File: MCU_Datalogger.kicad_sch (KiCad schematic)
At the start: 25 parts

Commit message: Schematic design complete
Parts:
- BT1: renamed from BT?; footprint (none) -> Connector_PinHeader_2.54mm:PinHeader_1x02_P2.54mm_Vertical
- C1, C4: renamed from C?; value C -> 0.1uF; footprint (none) -> Capacitor_SMD:C_0805_2012Metric_Pad1.18x1.45mm_HandSolder
- C2, C3: renamed from C?; value C -> 22pF; footprint (none) -> Capacitor_SMD:C_0805_2012Metric_Pad1.18x1.45mm_HandSolder
- C5: renamed from C?; value C_Polarized -> 100nF; footprint (none) -> Capacitor_SMD:C_0805_2012Metric_Pad1.18x1.45mm_HandSolder
- D1, D2: renamed from D?; footprint (none) -> LED_SMD:LED_0805_2012Metric_Pad1.15x1.40mm_HandSolder
- H1, H2, H3, H4: renamed from H?; footprint (none) -> MountingHole:MountingHole_2.1mm
- R1, R2, R6: renamed from R?; value R_US -> 10K; footprint (none) -> Resistor_SMD:R_0805_2012Metric_Pad1.20x1.40mm_HandSolder
- R3, R5: renamed from R?; value R_US -> 4.7K; footprint (none) -> Resistor_SMD:R_0805_2012Metric_Pad1.20x1.40mm_HandSolder
- R4, R7: renamed from R?; value R_US -> 330; footprint (none) -> Resistor_SMD:R_0805_2012Metric_Pad1.20x1.40mm_HandSolder
- U1: renamed from U?; footprint SOIC127P600X175-8N -> DS1337S_:SOIC127P600X175-8N
- U2, U3: renamed from U?; footprint (none) -> Package_SO:SOIC-8_5.23x5.23mm_P1.27mm
- U4: renamed from U?; footprint QFP80P900X900X120-32N -> ATMEGA328P-AU:QFP80P900X900X120-32N
- Y1: renamed from Y?; value Crystal -> 32.768 KHz; footprint (none) -> Crystal:Crystal_SMD_5032-2Pin_5.0x3.2mm_HandSoldering
- Y2: renamed from Y?; value Crystal -> 16 MHz; footprint (none) -> Crystal:Crystal_SMD_5032-2Pin_5.0x3.2mm_HandSoldering
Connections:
- net Vcc: now reaches R5.1
- net Vcc: now also C1.1, R1.1, R2.1, R3.1, R6.1, U1.8 (VCC), U2.1 (A0), U2.2 (A1), U2.3 (A2), U2.8 (VCC), U3.1 (A0), U3.3 (A2), U3.8 (VCC)
- net SDA: now reaches R5.2
- net SDA: now also U1.5 (SDA), U2.5 (SDA), U3.5 (SDA), U4.27 (PC4)
- net GND: now reaches C1.2
- net GND: now also BT1.2 (-), C2.1, C3.1, C4.1, C5.2, R4.1, R7.2, U1.4 (GND), U2.4 (GND), U2.7 (WP), U3.2 (A1), U3.4 (GND), U3.7 (WP), U4.21 (GND), U4.3 (GND), U4.5 (GND)
- net SCK: now reaches U2.6 (SCL)
- net SCK: now also D1.2 (A), R3.2, U1.6 (SCL), U3.6 (SCL), U4.17 (PB5), U4.28 (PC5)
- net at D1.1 (K): now also R4.2
- net at R7.1: now also D2.1 (K)
- net at U1.1 (X1): now also Y1.1
- net at U1.2 (X2): now also Y1.2
- net at U1.3 (~{INTA}): now also R1.2
- net at U1.7 (SQW/~{INT}): now also R2.2
- net at Y2.1: now also C3.2, U4.8 (PB7)
- net at Y2.2: now also C2.2, U4.7 (PB6)
- net D3: now reaches U4.1 (PD3)
- net D6: now reaches U4.10 (PD6)
- net D7: now reaches U4.11 (PD7)
- net D8: now reaches U4.12 (PB0)
- net MOSI: now reaches U4.15 (PB3)
- net MISO: now reaches U4.16 (PB4)
- net at U4.18 (AVCC): now also BT1.1 (+), C5.1, D2.2 (A), U4.4 (VCC)
- net D4: now reaches U4.2 (PD4)
- net at U4.20 (AREF): now also C4.2
- net RESET: now reaches U4.29 (PC6/~{RESET})
- net RESET: now also R6.2
- net RX: now reaches U4.30 (PD0)
- net TX: now reaches U4.31 (PD1)
- net D2: now reaches U4.32 (PD2)
- net at U4.6 (VCC): no longer U4.4 (VCC)
- net D5: now reaches U4.9 (PD5)
- no-connect marks 0 -> 9
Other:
- sheet Connectors ports: added D2, D3, D4, D5, D6, D7, D8, GND, MISO, MOSI, RESET, RX, SCK, SDA, TX, Vcc; removed none
- note added: "EEPROM"
- note added: "MCU"
- note added: "Real Time Clock"
- moved on the sheet: BT1, C1, C2, C3, C4, C5, D1, D2, H1, H2, H3, H4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

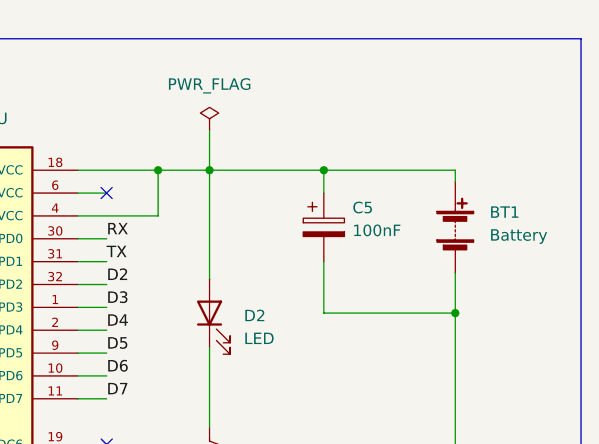
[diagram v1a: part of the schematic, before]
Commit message: 2 layer PCB design complete
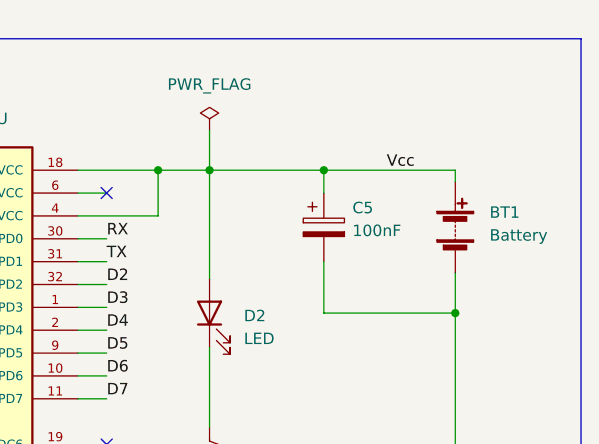
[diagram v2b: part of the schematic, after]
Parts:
- Y1, Y2: footprint Crystal:Crystal_SMD_5032-2Pin_5.0x3.2mm_HandSoldering -> ABM2-32:XTAL_ABM2-32.000MHZ-D4YF-T
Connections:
- net Vcc: now also BT1.1 (+), C5.1, D2.2 (A), U4.18 (AVCC), U4.4 (VCC)
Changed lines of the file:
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@@
+    (effects (font (size 1.27 1.27)) (justify left bottom))
+  )
+  (label "Vcc" (at 256.54 43.18 0)
     (effects (font (size 1.27 1.27)) (justify left bottom))
   )
@@
       (effects (font (size 1.27 1.27)) (justify right))
     )
-    (property "Footprint" "Crystal:Crystal_SMD_5032-2Pin_5.0x3.2mm_HandSoldering" (id 2) (at 169.545 71.755 0)
+    (property "Footprint" "ABM2-32:XTAL_ABM2-32.000MHZ-D4YF-T" (id 2) (at 169.545 71.755 0)
       (effects (font (size 1.27 1.27)) hide)
     )
@@
       (effects (font (size 1.27 1.27)) (justify left))
     )
-    (property "Footprint" "Crystal:Crystal_SMD_5032-2Pin_5.0x3.2mm_HandSoldering" (id 2) (at 21.59 69.85 0)
+    (property "Footprint" "ABM2-32:XTAL_ABM2-32.000MHZ-D4YF-T" (id 2) (at 21.59 69.85 0)
       (effects (font (size 1.27 1.27)) hide)
     )
@@
     )
     (path "/c96d047b-f1e3-4e27-aa7a-e20f3d748e34"
-      (reference "Y1") (unit 1) (value "32.768 KHz") (footprint "Crystal:Crystal_SMD_5032-2Pin_5.0x3.2mm_HandSoldering")
+      (reference "Y1") (unit 1) (value "32.768 KHz") (footprint "ABM2-32:XTAL_ABM2-32.000MHZ-D4YF-T")
     )
     (path "/780593a8-3f7b-4d23-9ea7-1f7af43d16ab"
-      (reference "Y2") (unit 1) (value "16 MHz") (footprint "Crystal:Crystal_SMD_5032-2Pin_5.0x3.2mm_HandSoldering")
-    )
-  )
+      (reference "Y2") (unit 1) (value "16 MHz") (footprint "ABM2-32:XTAL_ABM2-32.000MHZ-D4YF-T")
+    )
+  )

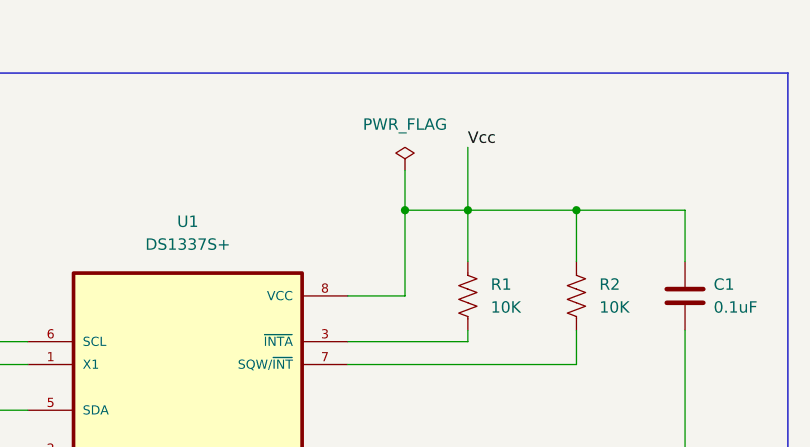
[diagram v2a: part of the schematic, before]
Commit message: Minor changes to PCB footprints
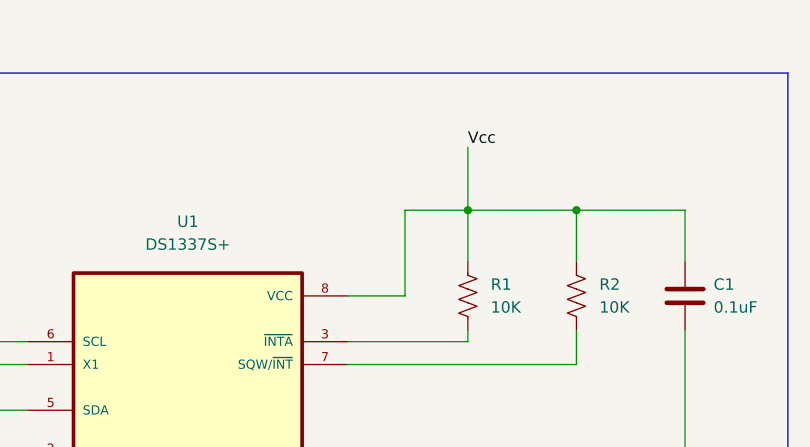
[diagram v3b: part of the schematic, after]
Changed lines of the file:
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@@
   (junction (at 169.545 76.835) (diameter 0) (color 0 0 0 0)
-  )
-  (junction (at 90.805 47.625) (diameter 0) (color 0 0 0 0)
   )
   (junction (at 146.685 53.34) (diameter 0) (color 0 0 0 0)
@@
   )
   (wire (pts (xy 197.485 129.54) (xy 181.61 129.54))
-    (stroke (width 0) (type default) (color 0 0 0 0))
-  )
-  (wire (pts (xy 90.805 43.18) (xy 90.805 47.625))
     (stroke (width 0) (type default) (color 0 0 0 0))
   )
@@
     (pin "1")
   )
-  (symbol (lib_id "power:PWR_FLAG") (at 90.805 43.18 0) (unit 1)
-    (in_bom yes) (on_board yes) (fields_autoplaced)
-    (property "Reference" "#FLG0103" (id 0) (at 90.805 41.275 0)
-      (effects (font (size 1.27 1.27)) hide)
-    )
-    (property "Value" "PWR_FLAG" (id 1) (at 90.805 38.1 0))
-    (property "Footprint" "" (id 2) (at 90.805 43.18 0)
-      (effects (font (size 1.27 1.27)) hide)
-    )
-    (property "Datasheet" "~" (id 3) (at 90.805 43.18 0)
-      (effects (font (size 1.27 1.27)) hide)
-    )
-    (pin "1")
-  )
   (symbol (lib_id "Device:R_US") (at 178.435 88.9 90) (unit 1)
     (in_bom yes) (on_board yes) (fields_autoplaced)
@@
       (reference "#FLG0102") (unit 1) (value "PWR_FLAG") (footprint "")
     )
-    (path "/f020a6f4-caee-4c19-8fba-99f271eb778b"
-      (reference "#FLG0103") (unit 1) (value "PWR_FLAG") (footprint "")
-    )
     (path "/e30ba7ec-fa95-461f-beca-d2c08d6124f6"

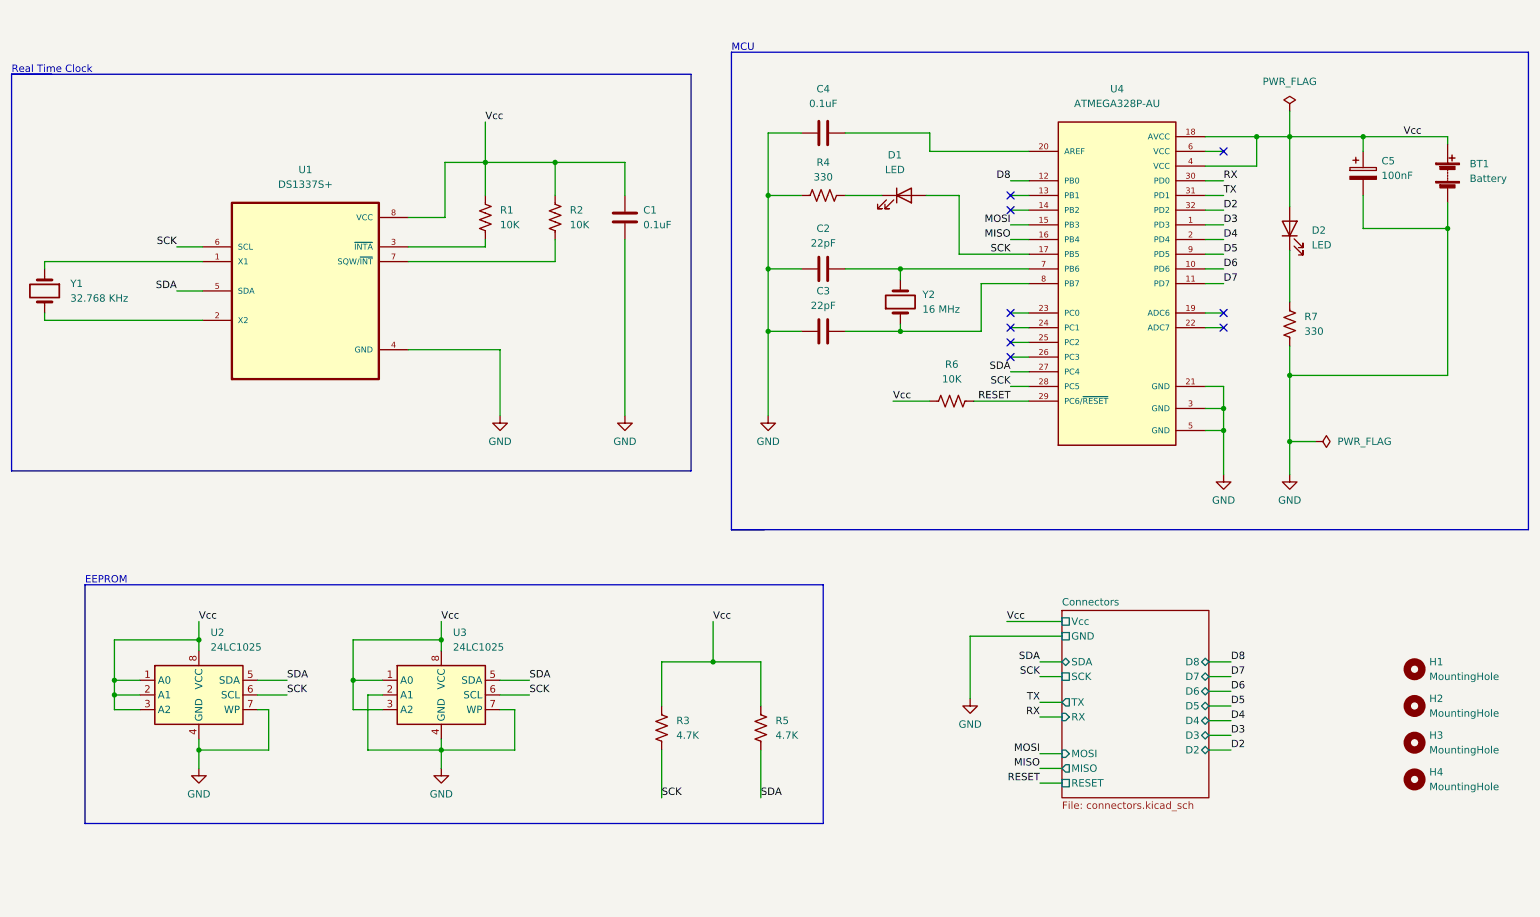
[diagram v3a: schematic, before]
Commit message: Added SCL net to schematic and fixed errors
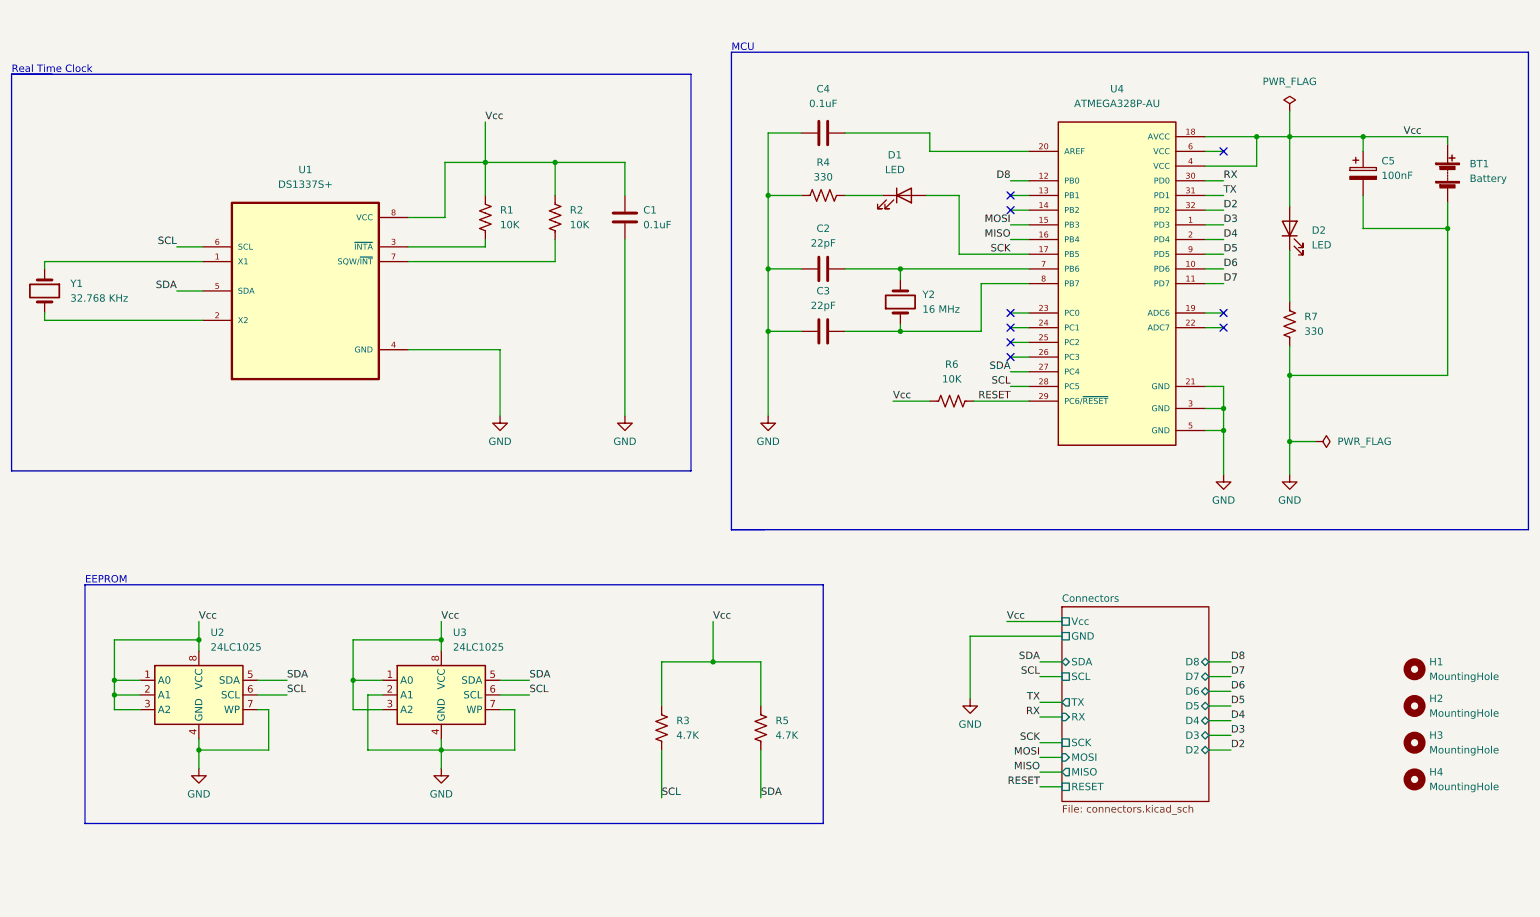
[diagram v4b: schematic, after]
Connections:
- net SCK: no longer R3.2, U1.6 (SCL), U2.6 (SCL), U3.6 (SCL), U4.28 (PC5)
- new net SCL: R3.2, U1.6 (SCL), U2.6 (SCL), U3.6 (SCL), U4.28 (PC5)
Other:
- sheet Connectors ports: added SCL; removed none
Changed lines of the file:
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@@
     (stroke (width 0) (type default) (color 0 0 0 0))
   )
-  (wire (pts (xy 193.675 154.94) (xy 197.485 154.94))
+  (wire (pts (xy 193.675 155.575) (xy 197.485 155.575))
     (stroke (width 0) (type default) (color 0 0 0 0))
   )
@@
     (stroke (width 0) (type default) (color 0 0 0 0))
   )
-  (wire (pts (xy 193.675 149.86) (xy 197.485 149.86))
+  (wire (pts (xy 193.675 150.495) (xy 197.485 150.495))
     (stroke (width 0) (type default) (color 0 0 0 0))
   )
@@
     (stroke (width 0) (type default) (color 0 0 0 0))
   )
-  (wire (pts (xy 193.675 152.4) (xy 197.485 152.4))
+  (wire (pts (xy 193.675 153.035) (xy 197.485 153.035))
     (stroke (width 0) (type default) (color 0 0 0 0))
   )
@@
     (stroke (width 0) (type default) (color 0 0 0 0))
   )
+  (wire (pts (xy 193.675 147.955) (xy 197.485 147.955))
+    (stroke (width 0) (type default) (color 0 0 0 0))
+  )
   (polyline (pts (xy 140.335 111.125) (xy 146.05 111.125))
     (stroke (width 0) (type default) (color 0 0 0 0))
@@
     (effects (font (size 1.27 1.27)) (justify left bottom))
   )
-  (label "SCK" (at 128.27 157.48 0)
+  (label "SCL" (at 128.27 157.48 0)
     (effects (font (size 1.27 1.27)) (justify left bottom))
   )
@@
     (effects (font (size 1.27 1.27)) (justify left bottom))
   )
-  (label "SCK" (at 188.595 86.36 180)
+  (label "SCL" (at 188.595 86.36 180)
     (effects (font (size 1.27 1.27)) (justify right bottom))
   )
@@
     (effects (font (size 1.27 1.27)) (justify left bottom))
   )
-  (label "SCK" (at 105.41 139.7 0)
+  (label "SCL" (at 105.41 139.7 0)
     (effects (font (size 1.27 1.27)) (justify left bottom))
   )
@@
     (effects (font (size 1.27 1.27)) (justify left bottom))
   )
-  (label "SCK" (at 63.5 139.7 0)
+  (label "SCL" (at 63.5 139.7 0)
     (effects (font (size 1.27 1.27)) (justify left bottom))
   )
@@
     (effects (font (size 1.27 1.27)) (justify left bottom))
   )
-  (label "SCK" (at 44.45 62.23 180)
-    (effects (font (size 1.27 1.27)) (justify right bottom))
-  )
-  (label "SCK" (at 193.675 136.525 180)
+  (label "SCL" (at 44.45 62.23 180)
+    (effects (font (size 1.27 1.27)) (justify right bottom))
+  )
+  (label "SCL" (at 193.675 136.525 180)
     (effects (font (size 1.27 1.27)) (justify right bottom))
   )
@@
     (effects (font (size 1.27 1.27)) (justify left bottom))
   )
-  (label "MISO" (at 193.675 152.4 180)
-    (effects (font (size 1.27 1.27)) (justify right bottom))
-  )
-  (label "RESET" (at 193.675 154.94 180)
+  (label "MISO" (at 193.675 153.035 180)
+    (effects (font (size 1.27 1.27)) (justify right bottom))
+  )
+  (label "RESET" (at 193.675 155.575 180)
     (effects (font (size 1.27 1.27)) (justify right bottom))
   )
@@
     (effects (font (size 1.27 1.27)) (justify left bottom))
   )
+  (label "SCK" (at 193.675 147.955 180)
+    (effects (font (size 1.27 1.27)) (justify right bottom))
+  )
   (label "TX" (at 193.675 140.97 180)
     (effects (font (size 1.27 1.27)) (justify right bottom))
   )
-  (label "MOSI" (at 193.675 149.86 180)
+  (label "MOSI" (at 193.675 150.495 180)
     (effects (font (size 1.27 1.27)) (justify right bottom))
   )
@@
     (pin "8")
   )
-  (sheet (at 197.485 125.095) (size 25.4 32.385) (fields_autoplaced)
+  (sheet (at 197.485 124.46) (size 25.4 33.655) (fields_autoplaced)
     (stroke (width 0.1524) (type solid) (color 0 0 0 0))
     (fill (color 0 0 0 0.0000))
-    (property "Sheet name" "Connectors" (id 0) (at 197.485 124.3834 0)
+    (property "Sheet name" "Connectors" (id 0) (at 197.485 123.7484 0)
       (effects (font (size 1.27 1.27)) (justify left bottom))
     )
-    (property "Sheet file" "connectors.kicad_sch" (id 1) (at 197.485 158.0646 0)
+    (property "Sheet file" "connectors.kicad_sch" (id 1) (at 197.485 158.6996 0)
       (effects (font (size 1.27 1.27)) (justify left top))
     )
@@
       (effects (font (size 1.27 1.27)) (justify right))
     )
-    (pin "SCK" passive (at 197.485 136.525 180)
-      (effects (font (size 1.27 1.27)) (justify left))
-    )
-    (pin "RESET" passive (at 197.485 154.94 180)
-      (effects (font (size 1.27 1.27)) (justify left))
-    )
-    (pin "MISO" output (at 197.485 152.4 180)
+    (pin "SCK" passive (at 197.485 147.955 180)
+      (effects (font (size 1.27 1.27)) (justify left))
+    )
+    (pin "RESET" passive (at 197.485 155.575 180)
+      (effects (font (size 1.27 1.27)) (justify left))
+    )
+    (pin "MISO" output (at 197.485 153.035 180)
       (effects (font (size 1.27 1.27)) (justify left))
     )
@@
       (effects (font (size 1.27 1.27)) (justify right))
     )
-    (pin "MOSI" input (at 197.485 149.86 180)
-      (effects (font (size 1.27 1.27)) (justify left))
-    )
+    (pin "MOSI" input (at 197.485 150.495 180)
+      (effects (font (size 1.27 1.27)) (justify left))
+    )
+    (pin "SCL" passive (at 197.485 136.525 180)
+      (effects (font (size 1.27 1.27)) (justify left))
+    )
